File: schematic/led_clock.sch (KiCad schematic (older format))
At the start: 11 parts, among them J1 CONN_01X15, J2 CONN_01X15, J3 CONN_01X04, J4 CONN_01X04, U1 SN74LVC2T45

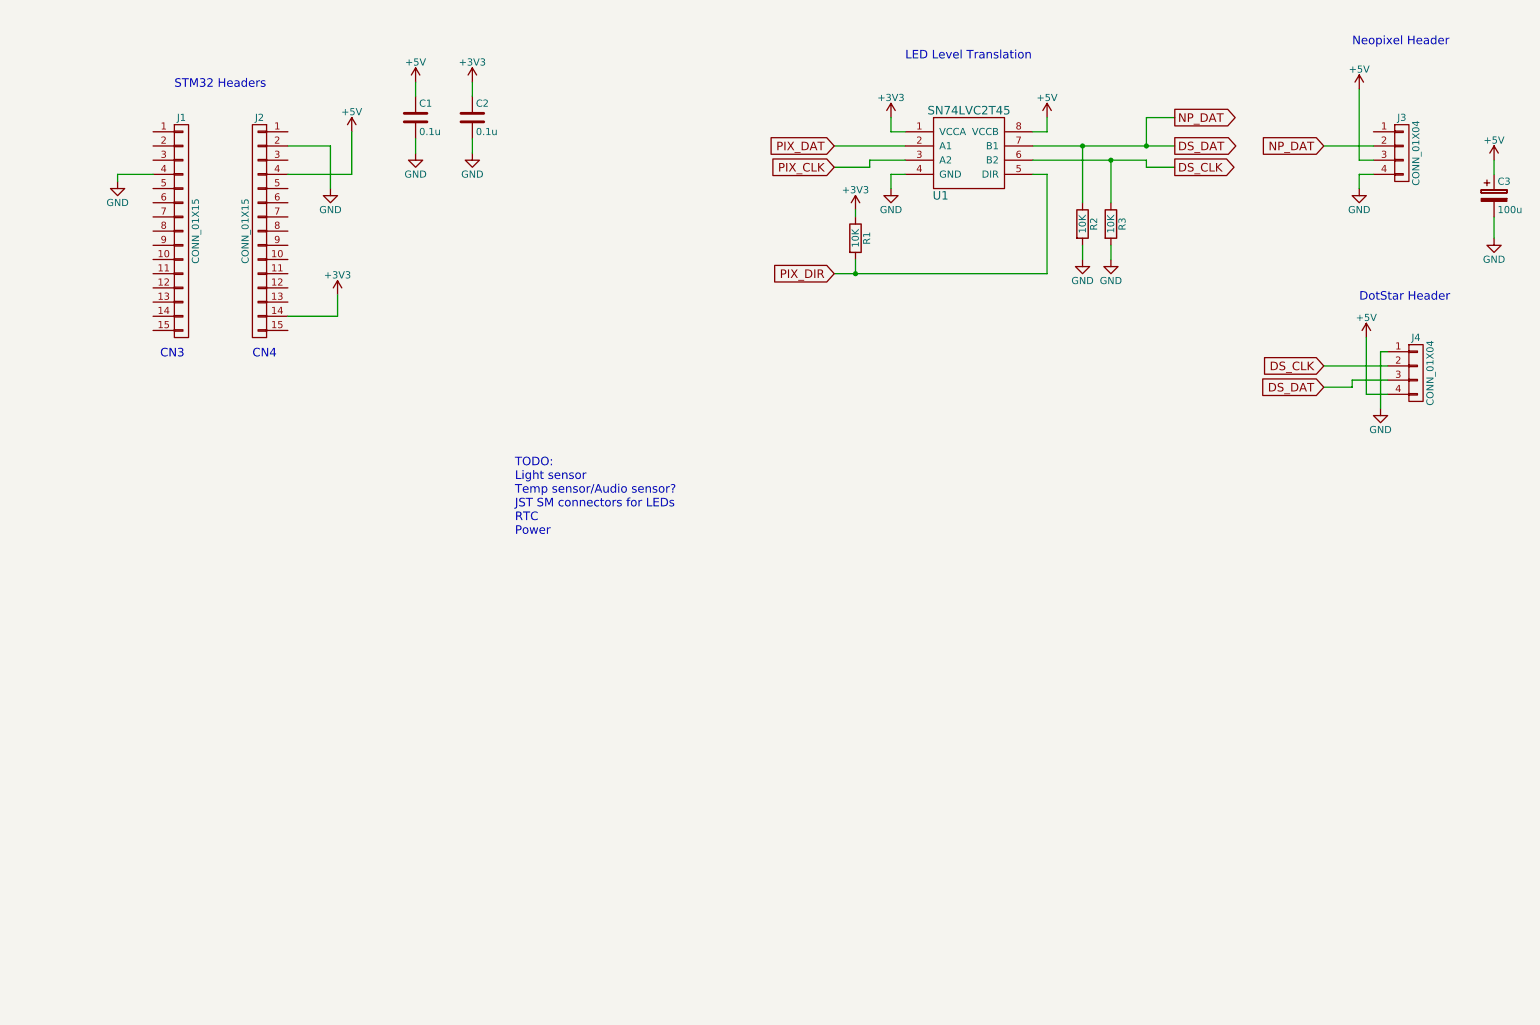
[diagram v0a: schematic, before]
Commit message: Add sensors to schematic
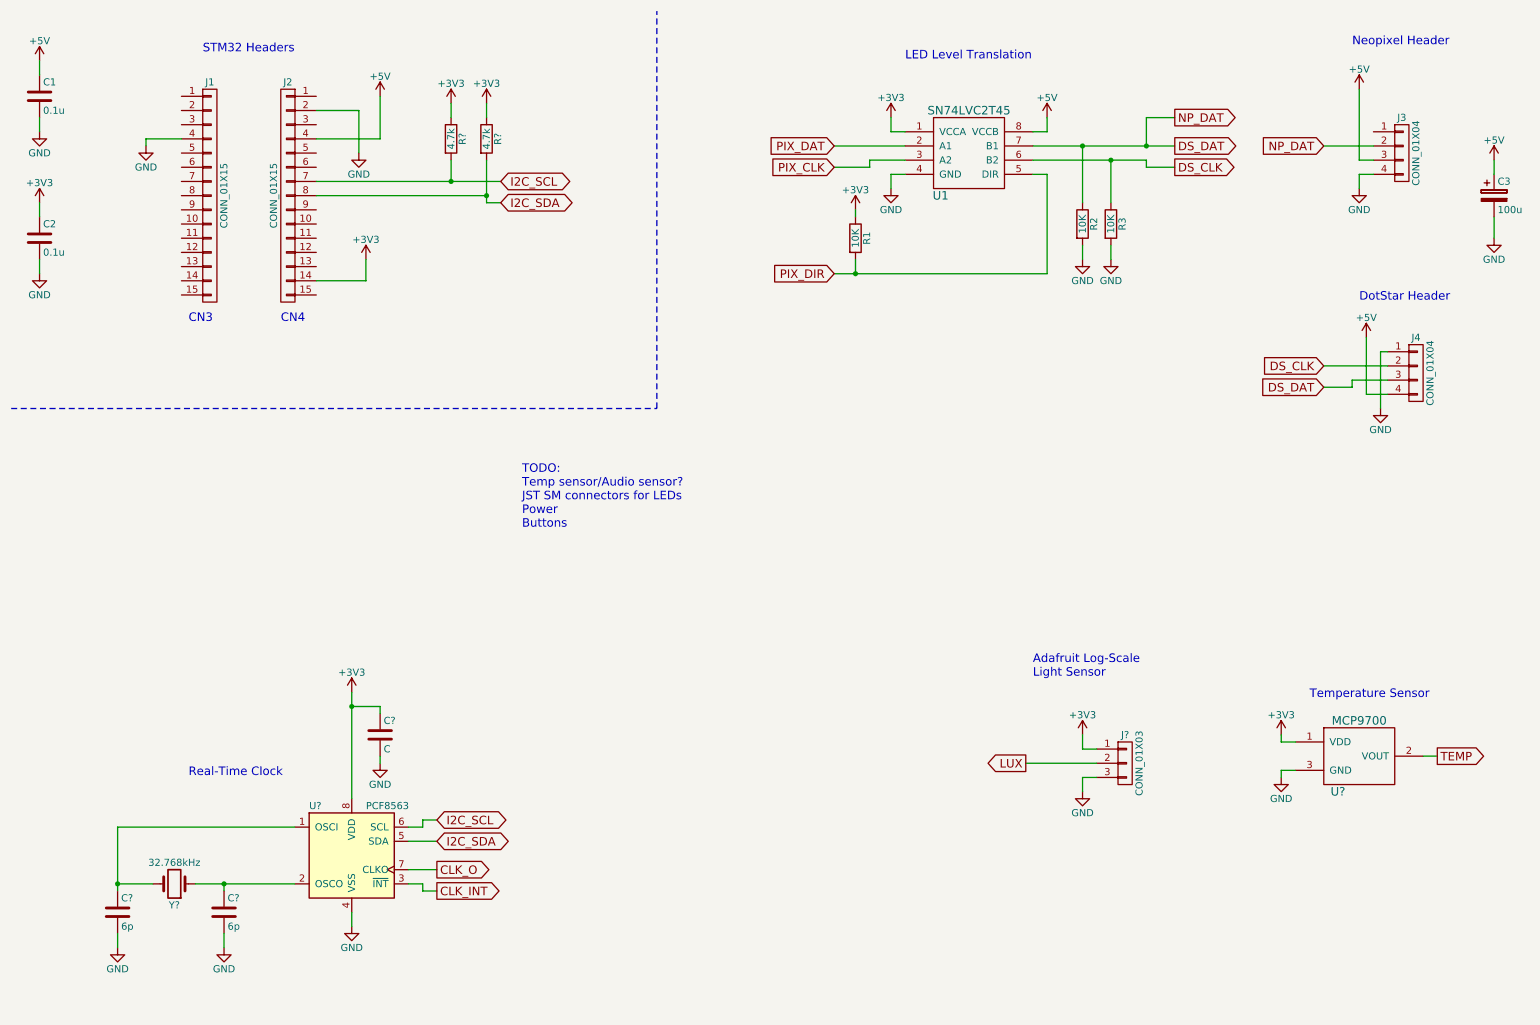
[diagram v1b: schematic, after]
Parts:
- added C?: C, symbol C
- added C? (x2): 6p, symbol C
- added J?: CONN_01X03, symbol CONN_01X03
- added R? (x2): 4.7k, symbol R
- added U?: MCP9700, symbol MCP9700
- added U?: PCF8563, symbol PCF8563
- added Y?: 32.768kHz, symbol Crystal
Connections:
- net +3V3: now also C?.1, J?.1 (P1), R?.1, R?.1, U?.1 (VDD), U?.8 (VDD)
- net GND: now also C?.2, C?.2, C?.2, J?.3 (P3), U?.3 (GND), U?.4 (VSS)
- net I2C_SCL: now reaches J2.7 (P7)
- net I2C_SCL: now also R?.2, U?.6 (SCL)
- net I2C_SDA: now reaches J2.8 (P8)
- net I2C_SDA: now also R?.2, U?.5 (SDA)
- new net: C?.1, U?.1 (OSCI), Y?.2
- new net: C?.1, U?.2 (OSCO), Y?.1
- new net CLK_INT: U?.3 (~INT~)
- new net CLK_O: U?.7 (CLKO)
- new net LUX: J?.2 (P2)
- new net TEMP: U?.2 (VOUT)
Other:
- note added: "Adafruit Log-Scale\nLight Sensor"
- note added: "Real-Time Clock"
- note added: "TODO:\nTemp sensor/Audio sensor?\nJST SM connectors for LEDs\nPower\nButtons"
- note added: "Temperature Sensor"
- note removed: "TODO:\nLight sensor\nTemp sensor/Audio sensor?\nJST SM connectors for LEDs\nRTC\nPower"
- moved on the sheet: C1, C2, J1, J2

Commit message: Rev 1.0 of circuit boards
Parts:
- removed J1, J2: CONN_01X15, Pin_Headers:Pin_Header_Straight_1x15_Pitch2.54mm, symbol CONN_01X15
- removed U1: SN74LVC2T45, Housings_SSOP:MSOP-8_3x3mm_Pitch0.65mm, symbol SN74LVC2T45
- added BT1: Battery_Cell, symbol Battery_Cell
- added C10, C11, C7, C8, C9: 0.1u, Capacitors_SMD:C_0603, symbol C
- added D1: D, Diodes_SMD:D_0603, symbol D
- added J1: CONN_01X08, symbol CONN_01X08
- added J2: CONN_01X06, symbol CONN_01X06
- added J5: USB_OTG, Connectors:USB_Micro-B, symbol USB_OTG
- added J7: CONN_01X02, Pin_Headers:Pin_Header_Straight_1x02_Pitch2.54mm, symbol CONN_01X02
- added R6: 10K, Resistors_SMD:R_0603, symbol R
- added SW1: Rotary_Encoder_Switch, symbol Rotary_Encoder_Switch
- added U1, U5: SN74LVC1T45, TO_SOT_Packages_SMD:SOT-23-6, symbol SN74LVC1T45
- added U2: Nucleo32, led_clock_footprints:Nucleo32, symbol Nucleo32
- C4, C5: renamed from C?; footprint (none) -> Capacitors_SMD:C_0603
- C6: renamed from C?; value C -> 0.1u; footprint (none) -> Capacitors_SMD:C_0603
- J6: renamed from J?; footprint (none) -> Pin_Headers:Pin_Header_Straight_1x03_Pitch2.54mm
- R4, R5: renamed from R?; footprint (none) -> Resistors_SMD:R_0603
- U3: renamed from U?; footprint (none) -> Housings_SOIC:SOIC-8-1EP_3.9x4.9mm_Pitch1.27mm
- U4: renamed from U?; value MCP9700 -> MCP9701; footprint (none) -> TO_SOT_Packages_SMD:SOT-23
- gave numbers to parts that had none: 1
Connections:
- net +3V3: now also C11.1, C7.1, C8.1, D1.1 (K), U1.1 (VCCA), U2.14 (+3V3), U5.1 (VCCA)
- net +5V: now also J3.2 (P2), C10.1, C9.1, J5.1 (VBUS), J7.2 (P2), U1.6 (VCCB), U2.4 (+5V), U5.6 (VCCB); no longer J3.3 (P3)
- net DS_CLK: now also U5.4 (B1)
- net DS_DAT: now also J3.3 (P3), U1.4 (B1); no longer J3.2 (P2)
- net GND: now also J3.1 (P1), BT1.2 (-), C10.2, C11.2, C7.2, C8.2, C9.2, J5.5 (GND), J7.1 (P1), R6.2, SW1.2 (C), SW1.5, U1.2 (GND), U2.19 (GND), U2.2 (GND), U5.2 (GND); no longer J3.4 (P4)
- net I2C_SCL: now also U2.7 (A5)
- net I2C_SDA: now also U2.8 (A4)
- net LUX: now also U2.10 (A2)
- net PIX_CLK: now also U2.15 (D13), U5.3 (A1)
- net PIX_DAT: now also U1.3 (A1), U2.29 (D11)
- net PIX_DIR: now also U1.5 (DIR), U2.27 (D9), U5.5 (DIR)
- net TEMP: now also U2.11 (A1)
- new net: J5.6 (Shield), R6.1
- new net: BT1.1 (+), D1.2 (A)
- new net ROT_A: SW1.1 (A)
- new net ROT_B: SW1.3 (B)
- new net ROT_SW: SW1.4
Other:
- note added: "Adafruit Log-Scale\nLight Sensor\n(P/N 1384)"
- note added: "Digital Output"
- note added: "NUCLEO-L432KC"
- note added: "TODO: Test point for CLKO?"
- note added: "TODO: Use NCP360 here?"
- note added: "UART"
- note added: "USB (Power Only)"
- note removed: "Adafruit Log-Scale\nLight Sensor"
- moved on the sheet: C1, C2, C3, C4, C5, C6, J4, R1, R2, R3, R4, R5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
